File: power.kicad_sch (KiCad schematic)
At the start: 0 parts

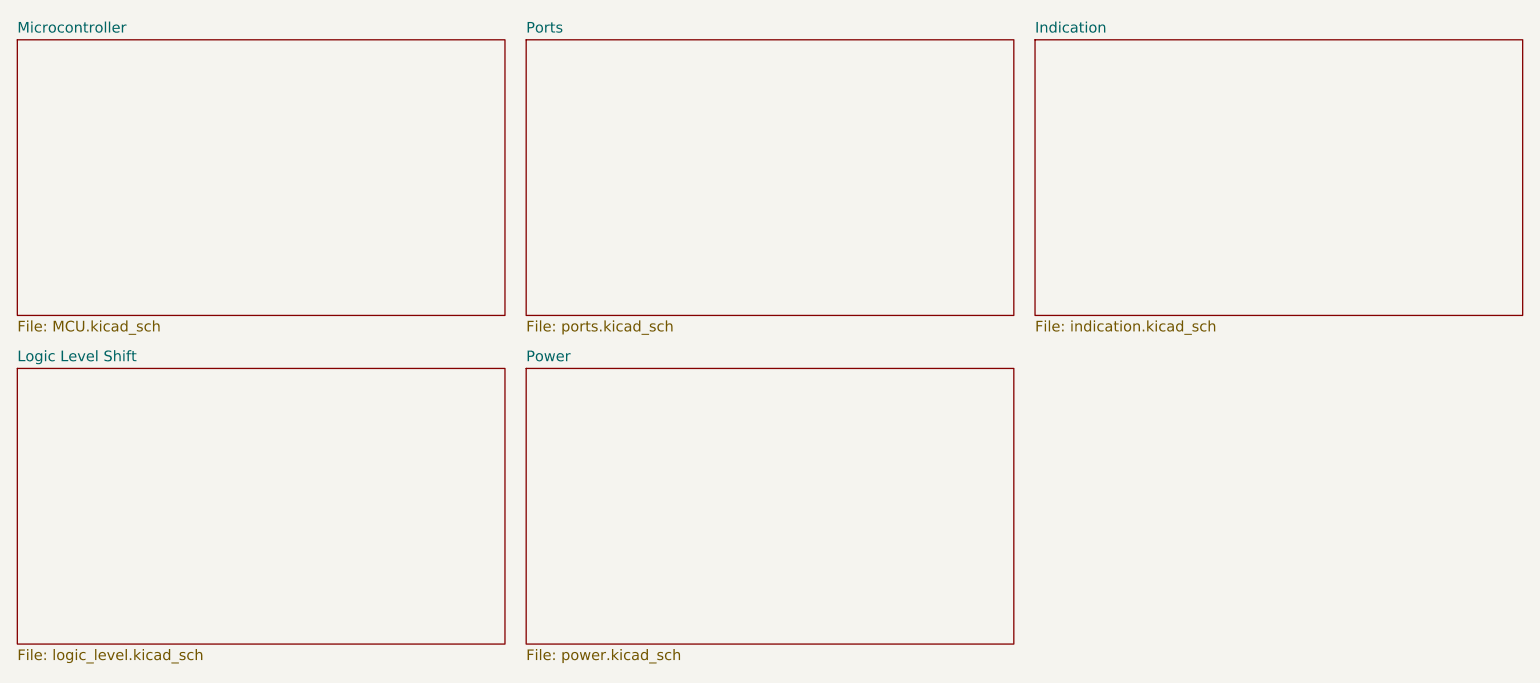
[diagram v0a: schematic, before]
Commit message: Break up schematic into hierarchical sheets
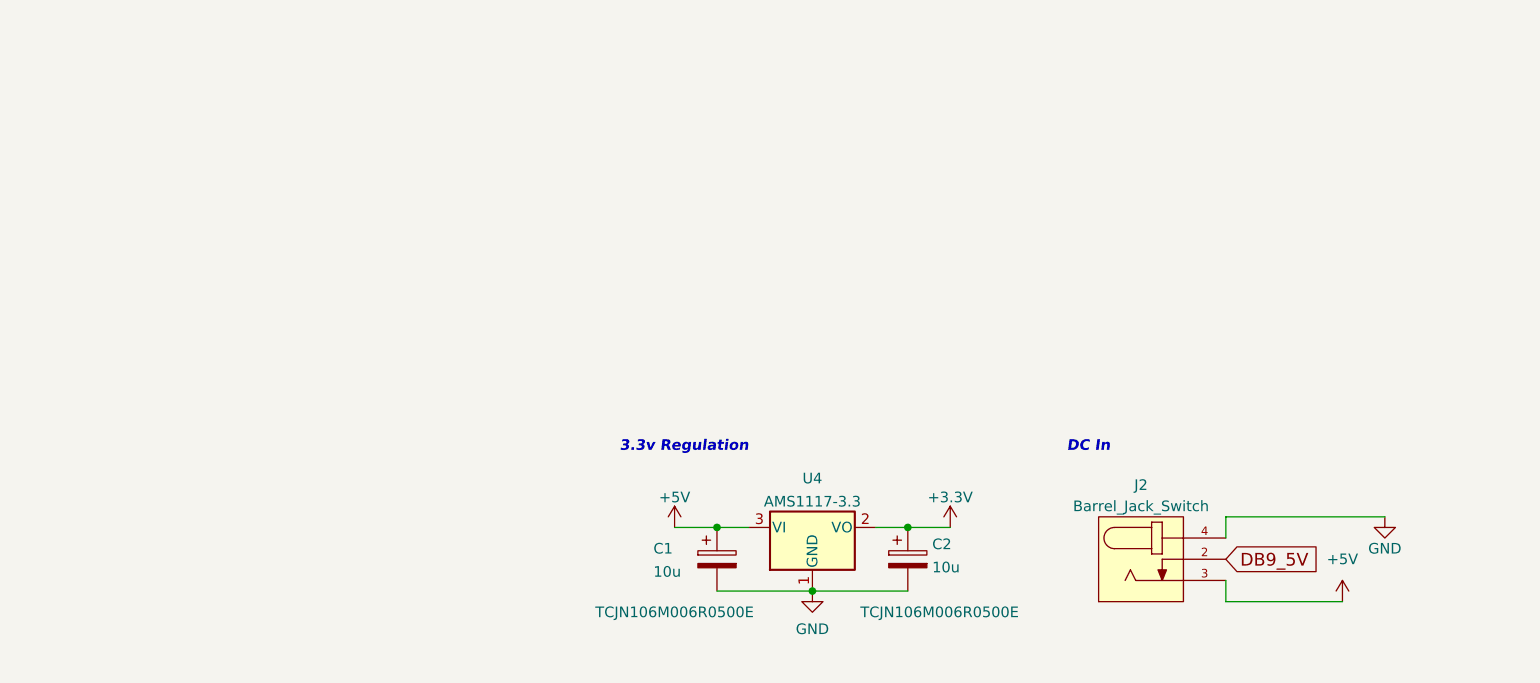
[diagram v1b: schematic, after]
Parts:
- added C1, C2: 10u, Capacitor_SMD:C_0805_2012Metric, symbol Device:C_Polarized
- added J2: Barrel_Jack_Switch, Library:NINIGI_DC-005, symbol LSF0108:DC-005
- added U4: AMS1117-3.3, Package_TO_SOT_SMD:SOT-223-3_TabPin2, symbol Regulator_Linear:AMS1117-3.3
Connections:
- new net +3V3: C2.1, U4.2 (VO)
- new net +5V: C1.1, J2.3, U4.3 (VI)
- new net DB9_5V: J2.2
- new net GND: C1.2, C2.2, J2.4, U4.1 (GND)
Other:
- removed sheet Indication
- removed sheet Logic Level Shift
- removed sheet Microcontroller
- removed sheet Ports
- removed sheet Power
- note added: "3.3v Regulation"
- note added: "DC In"
